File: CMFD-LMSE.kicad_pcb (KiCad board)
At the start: 2 copper layers, 130 parts, among them J1 Conn_01x02, J10 Conn_01x02, J11 Conn_01x02, J12 Conn_01x02, J2 Conn_01x02, J3 ZX62-B-5PA_33_, J4 Conn_01x02, J5 Conn_01x05, J6 Conn_01x02, J7 Conn_01x02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

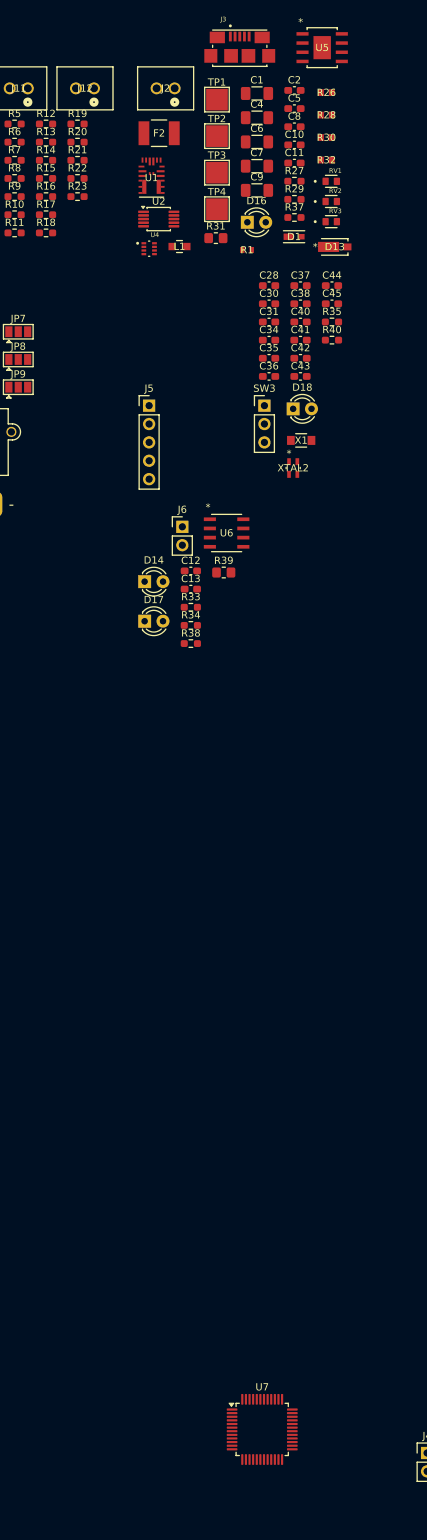
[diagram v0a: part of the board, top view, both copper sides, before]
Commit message: バイパスコンデンサ37~41
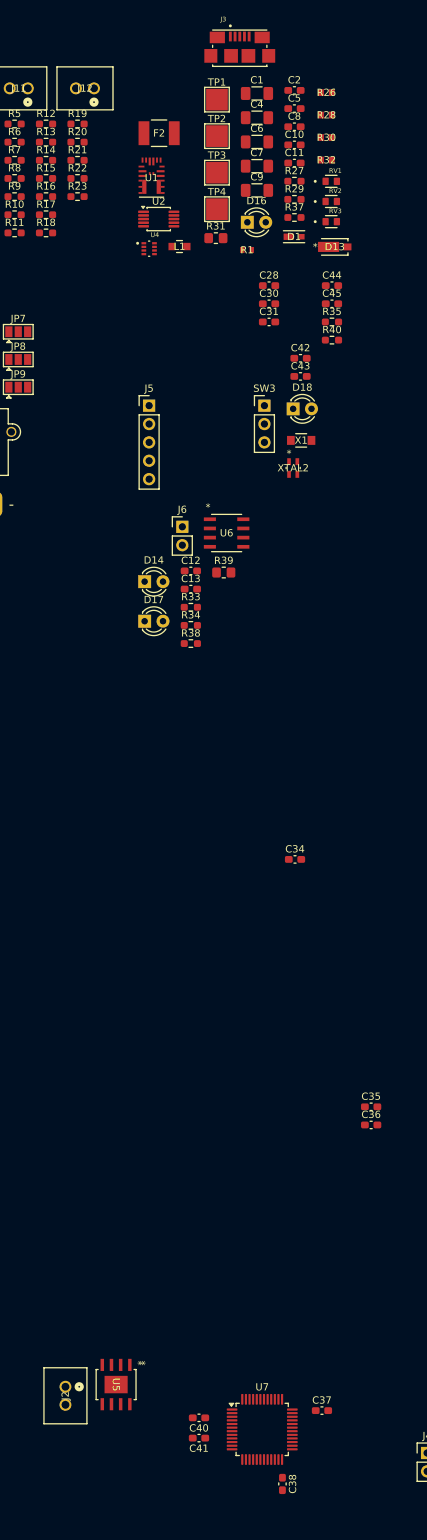
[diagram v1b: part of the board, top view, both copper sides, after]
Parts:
- moved U5 187.0 mm to (67.2, 99.6), turned to -90 degrees
- moved J2 180.1 mm to (60.2, 99.9), turned to 90 degrees
- moved C38 163.2 mm to (90.2, 113.3), turned to -90 degrees
- moved C37 155.6 mm to (95.7, 103.2)
- moved C41 152.4 mm to (78.7, 107.0), turned to 180 degrees
- moved C40 152.2 mm to (78.7, 104.2), turned to 180 degrees
- moved C35 104.4 mm to (102.5, 61.2)
- moved C36 104.4 mm to (102.5, 63.7)
- moved C34 71.9 mm to (91.9, 27.0)
